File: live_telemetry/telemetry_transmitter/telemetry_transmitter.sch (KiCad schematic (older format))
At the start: 15 parts, among them J1 Programming Header, U1 PIC18F26K83, U2 MCP2562, Y1 Crystal

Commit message: Change mcu to power off 3v3 and add LRN LED/SW
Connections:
- net +5V: no longer C1.1, R1.2, U1.20 (VDD), U2.5 (VIO)
- new net +3V3: C1.1, R1.2, U1.20 (VDD), U2.5 (VIO)
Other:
- note removed: "Should VIO be 3V3 not 5V?"
- moved on the sheet: C2
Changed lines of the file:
@@
 Wire Wire Line
 	5100 3000 4700 3000
-$Comp
-L power:+5V #PWR0101
-U 1 1 5DB51D90
-P 4700 2650
-F 0 "#PWR0101" H 4700 2500 50  0001 C CNN
-F 1 "+5V" H 4715 2823 50  0000 C CNN
-F 2 "" H 4700 2650 50  0001 C CNN
-F 3 "" H 4700 2650 50  0001 C CNN
-	1    4700 2650
-	1    0    0    -1
-$EndComp
-$Comp
-L power:+5V #PWR0102
-U 1 1 5DB54163
-P 6550 2650
-F 0 "#PWR0102" H 6550 2500 50  0001 C CNN
-F 1 "+5V" H 6565 2823 50  0000 C CNN
-F 2 "" H 6550 2650 50  0001 C CNN
-F 3 "" H 6550 2650 50  0001 C CNN
-	1    6550 2650
-	1    0    0    -1
-$EndComp
 Wire Wire Line
 	4700 3000 4700 2950
@@
 L Device:C C2
 U 1 1 5DB79E78
-P 8700 5150
-F 0 "C2" H 8815 5196 50  0000 L CNN
-F 1 "10u" H 8815 5105 50  0000 L CNN
-F 2 "" H 8738 5000 50  0001 C CNN
-F 3 "~" H 8700 5150 50  0001 C CNN
-	1    8700 5150
+P 8600 5150
+F 0 "C2" H 8715 5196 50  0000 L CNN
+F 1 "10u" H 8715 5105 50  0000 L CNN
+F 2 "" H 8638 5000 50  0001 C CNN
+F 3 "~" H 8600 5150 50  0001 C CNN
+	1    8600 5150
 	1    0    0    -1
 $EndComp
@@
 L power:GND #PWR0106
 U 1 1 5DB7A312
-P 8700 5350
-F 0 "#PWR0106" H 8700 5100 50  0001 C CNN
-F 1 "GND" H 8705 5177 50  0000 C CNN
-F 2 "" H 8700 5350 50  0001 C CNN
-F 3 "" H 8700 5350 50  0001 C CNN
-	1    8700 5350
-	1    0    0    -1
-$EndComp
-Wire Wire Line
-	8700 5300 8700 5350
+P 8600 5350
+F 0 "#PWR0106" H 8600 5100 50  0001 C CNN
+F 1 "GND" H 8605 5177 50  0000 C CNN
+F 2 "" H 8600 5350 50  0001 C CNN
+F 3 "" H 8600 5350 50  0001 C CNN
+	1    8600 5350
+	1    0    0    -1
+$EndComp
+Wire Wire Line
+	8600 5300 8600 5350
 $Comp
 L power:+5V #PWR0107
 U 1 1 5DB7C40F
-P 8700 4550
-F 0 "#PWR0107" H 8700 4400 50  0001 C CNN
-F 1 "+5V" H 8715 4723 50  0000 C CNN
-F 2 "" H 8700 4550 50  0001 C CNN
-F 3 "" H 8700 4550 50  0001 C CNN
-	1    8700 4550
+P 8600 4550
+F 0 "#PWR0107" H 8600 4400 50  0001 C CNN
+F 1 "+5V" H 8615 4723 50  0000 C CNN
+F 2 "" H 8600 4550 50  0001 C CNN
+F 3 "" H 8600 4550 50  0001 C CNN
+	1    8600 4550
 	1    0    0    -1
 $EndComp
@@
 	6550 3700 8250 3700
 Wire Wire Line
-	8900 4650 8800 4650
-Wire Wire Line
-	8700 4550 8700 4650
-Connection ~ 8700 4650
-Wire Wire Line
-	8700 4650 8700 5000
+	8600 4550 8600 4650
+Connection ~ 8600 4650
+Wire Wire Line
+	8600 4650 8600 5000
 Wire Wire Line
 	8900 4750 8800 4750
-Wire Wire Line
-	8800 4750 8800 4650
-Connection ~ 8800 4650
-Wire Wire Line
-	8800 4650 8700 4650
 $Comp
 L power:+5V #PWR0110
@@
 Wire Wire Line
 	2000 3400 2000 3200
-Text Notes 8850 5400 0    50   ~ 0
-Should VIO be 3V3 not 5V?
 Text Label 4550 3000 2    50   ~ 0
 ~MCLR
@@
 Text Notes 7100 6950 0    50   ~ 0
 The purpose of the telemetry transmitter board is to take in data from\n the can bus and transmit this data to the telemetry receiver board. \nThe telemetry transmitter board will then transmit this data via a RF module.
+$Comp
+L power:+3V3 #PWR0101
+U 1 1 5DE42E6B
+P 4700 2650
+F 0 "#PWR0101" H 4700 2500 50  0001 C CNN
+F 1 "+3V3" H 4715 2823 50  0000 C CNN
+F 2 "" H 4700 2650 50  0001 C CNN
+F 3 "" H 4700 2650 50  0001 C CNN
+	1    4700 2650
+	1    0    0    -1
+$EndComp
+$Comp
+L power:+3V3 #PWR0102
+U 1 1 5DE4639A
+P 6550 2650
+F 0 "#PWR0102" H 6550 2500 50  0001 C CNN
+F 1 "+3V3" H 6565 2823 50  0000 C CNN
+F 2 "" H 6550 2650 50  0001 C CNN
+F 3 "" H 6550 2650 50  0001 C CNN
+	1    6550 2650
+	1    0    0    -1
+$EndComp
+$Comp
+L power:+3V3 #PWR0126
+U 1 1 5DE483B0
+P 8800 4550
+F 0 "#PWR0126" H 8800 4400 50  0001 C CNN
+F 1 "+3V3" H 8815 4723 50  0000 C CNN
+F 2 "" H 8800 4550 50  0001 C CNN
+F 3 "" H 8800 4550 50  0001 C CNN
+	1    8800 4550
+	1    0    0    -1
+$EndComp
+Wire Wire Line
+	8600 4650 8900 4650
+Wire Wire Line
+	8800 4550 8800 4750
 $EndSCHEMATC

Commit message: Fix voltage mismatches, LED voltages, and add relative file path for canlib
-Programming header switched from 5V to 3V3
-LEDs switched from 5V to 3V3
-Relative file path added for transmitter and receiver for canlib
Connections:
- net +3V3: now also D1.2 (A), D2.2 (A), D3.2 (A), J1.4 (Pin_4)
- net +5V: no longer D1.2 (A), D2.2 (A), D3.2 (A), J1.4 (Pin_4)
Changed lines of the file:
@@
 EESchema Schematic File Version 4
+LIBS:telemetry_transmitter-cache
 EELAYER 29 0
 EELAYER END
@@
 Wire Wire Line
 	8900 4750 8800 4750
-$Comp
-L power:+5V #PWR0110
-U 1 1 5DC7920B
-P 2400 1700
-F 0 "#PWR0110" H 2400 1550 50  0001 C CNN
-F 1 "+5V" H 2415 1873 50  0000 C CNN
-F 2 "" H 2400 1700 50  0001 C CNN
-F 3 "" H 2400 1700 50  0001 C CNN
-	1    2400 1700
-	1    0    0    -1
-$EndComp
 Wire Wire Line
 	2050 2050 2400 2050
@@
 	0    -1   -1   0
 $EndComp
-$Comp
-L power:+5V #PWR0111
-U 1 1 5DC96631
-P 2350 3150
-F 0 "#PWR0111" H 2350 3000 50  0001 C CNN
-F 1 "+5V" H 2365 3323 50  0000 C CNN
-F 2 "" H 2350 3150 50  0001 C CNN
-F 3 "" H 2350 3150 50  0001 C CNN
-	1    2350 3150
-	1    0    0    -1
-$EndComp
-Wire Wire Line
-	2000 3400 2000 3200
 Text Label 4550 3000 2    50   ~ 0
 ~MCLR
@@
 Wire Wire Line
 	2350 3200 2350 3400
-Wire Wire Line
-	2000 3200 2350 3200
 Wire Wire Line
 	2700 3400 2700 3200
@@
 Wire Wire Line
 	8800 4550 8800 4750
+$Comp
+L power:+3V3 #PWR?
+U 1 1 5E043275
+P 2350 3150
+F 0 "#PWR?" H 2350 3000 50  0001 C CNN
+F 1 "+3V3" H 2365 3323 50  0000 C CNN
+F 2 "" H 2350 3150 50  0001 C CNN
+F 3 "" H 2350 3150 50  0001 C CNN
+	1    2350 3150
+	1    0    0    -1
+$EndComp
+$Comp
+L power:+3V3 #PWR?
+U 1 1 5E04875A
+P 2400 1700
+F 0 "#PWR?" H 2400 1550 50  0001 C CNN
+F 1 "+3V3" H 2415 1873 50  0000 C CNN
+F 2 "" H 2400 1700 50  0001 C CNN
+F 3 "" H 2400 1700 50  0001 C CNN
+	1    2400 1700
+	1    0    0    -1
+$EndComp
+Wire Wire Line
+	2000 3400 2000 3200
+Wire Wire Line
+	2000 3200 2350 3200
 $EndSCHEMATC

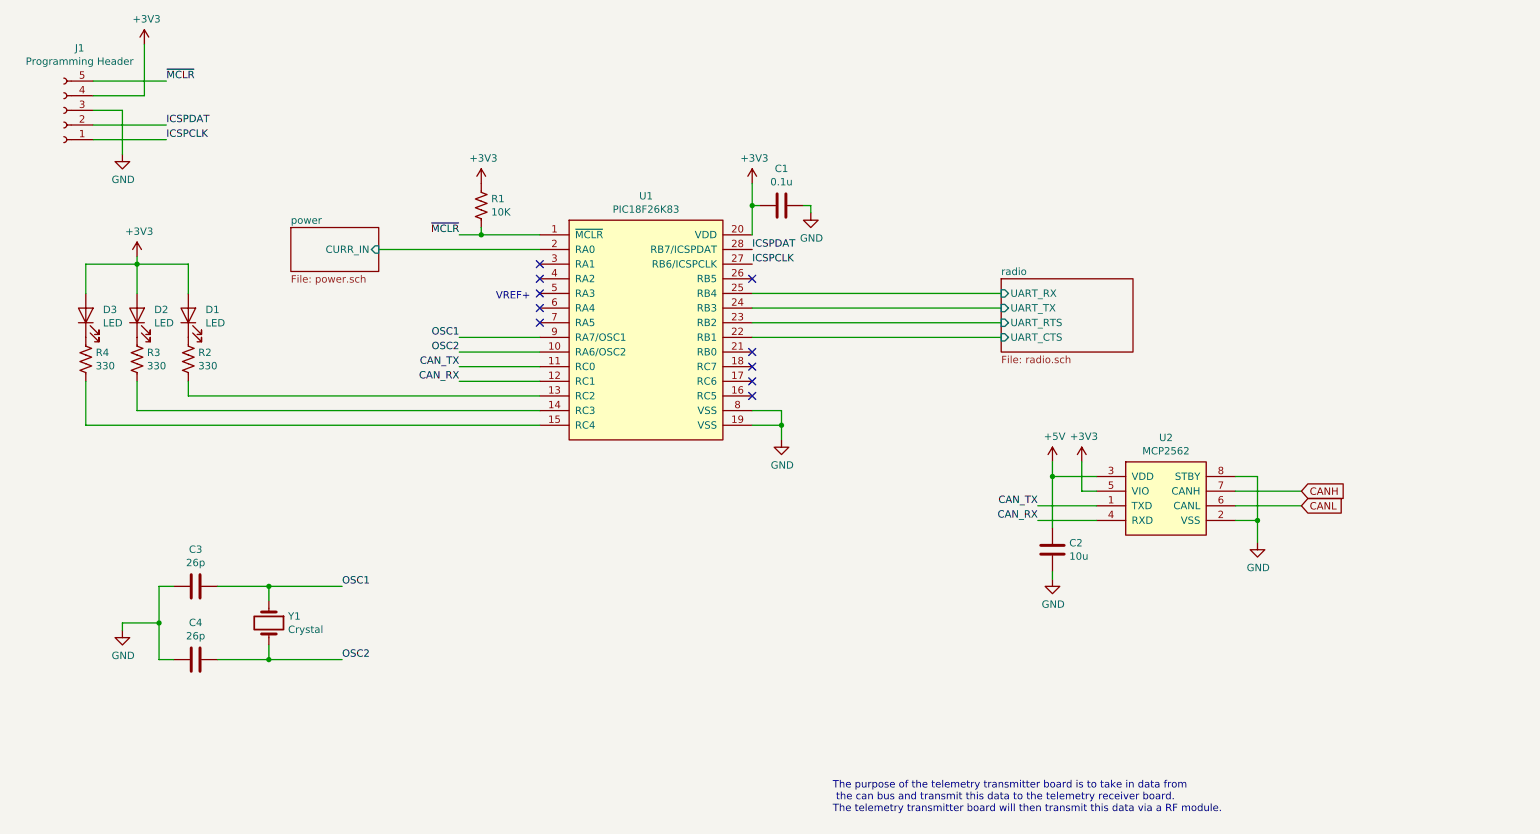
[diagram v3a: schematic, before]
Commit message: Addresses Adam/Aaron's comments: change RF module and take over for radio
Now that the CAN bus battery is going in the recovery electronics bay,
the telemetry_transmitter board will be taking over for radio for all
communication from RLCS to the rocket and will also handle the power
control of the CAN bus.
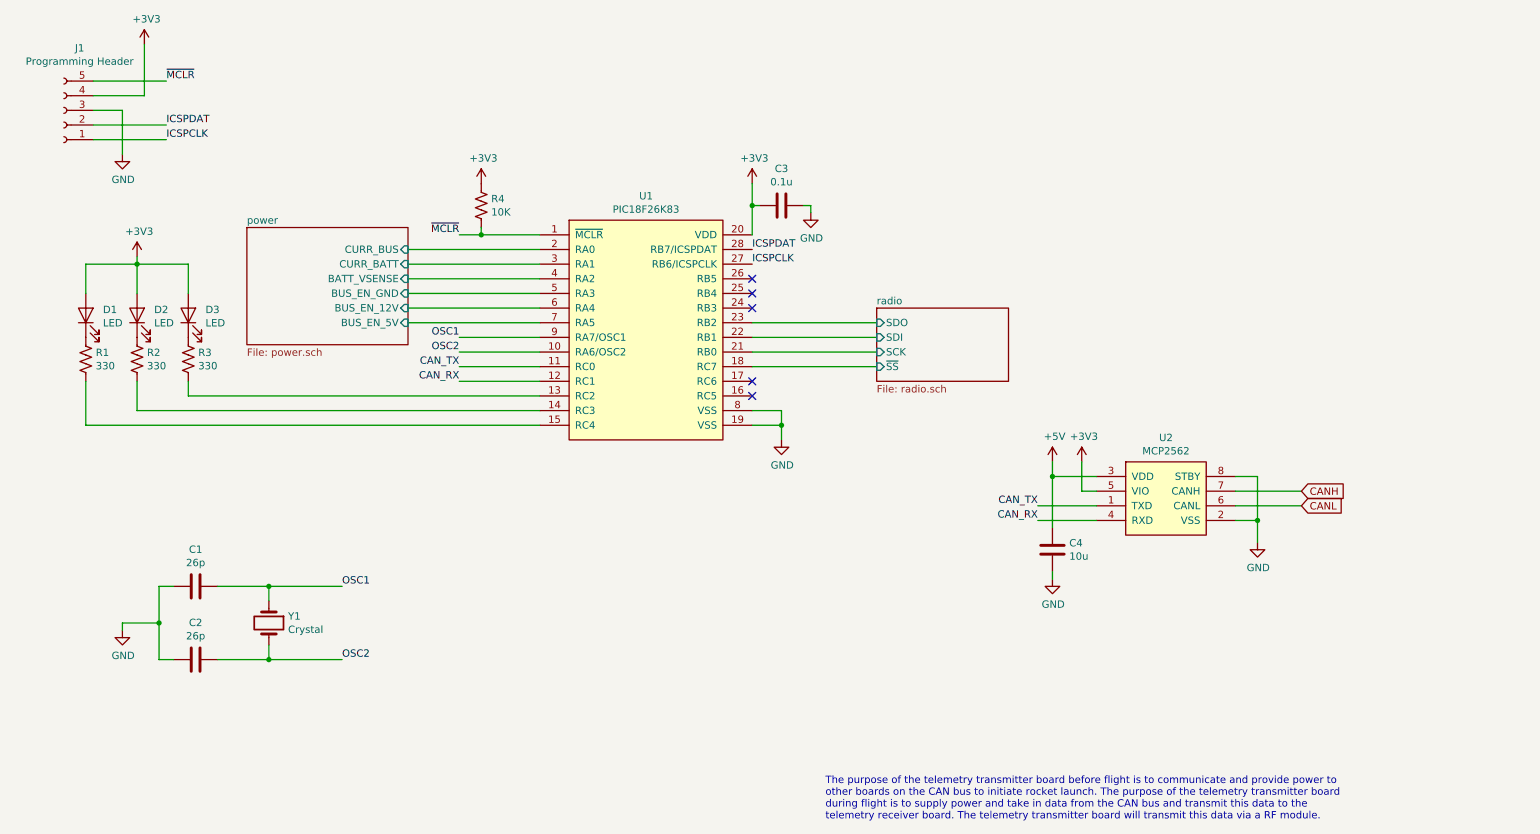
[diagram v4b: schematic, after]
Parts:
- renumbered C3 to C1, C4 to C2, C1 to C3, C2 to C4, D3 to D1, D1 to D3, R4 to R1, R3 to R2, R2 to R3, R1 to R4
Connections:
- net radio/~SS: now reaches U1.18 (RC7)
- net radio/SCK: now reaches U1.21 (RB0)
- net power/CURR_BATT: now reaches U1.3 (RA1)
- net power/BATT_VSENSE: now reaches U1.4 (RA2)
- net power/BUS_EN_GND: now reaches U1.5 (RA3)
- net power/BUS_EN_12V: now reaches U1.6 (RA4)
- net power/BUS_EN_5V: now reaches U1.7 (RA5)
- net power/CURR_IN renamed power/CURR_BUS
- net radio/UART_CTS renamed radio/SDI
- net radio/UART_RTS renamed radio/SDO
- net radio/UART_RX: no longer names the net of U1.25 (RB4)
- net radio/UART_TX: no longer names the net of U1.24 (RB3)
- no-connect marks 10 -> 5
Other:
- note added: "The purpose of the telemetry transmitter board before flight is to communicate and provide power to \nother boards on the CAN bus to initiate rocket launch. The purpose of the telemetry transmitter board\nduring flight is to supply power and take in data from the CAN bus and transmit this data to the \ntelemetry receiver board. The telemetry transmitter board will transmit this data via a RF modu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"
- note removed: "The purpose of the telemetry transmitter board is to take in data from\n the can bus and transmit this data to the telemetry receiver board. \nThe telemetry transmitter board will then transmit this data via a RF module."
- note removed: "VREF+"
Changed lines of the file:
@@
 	4700 3000 4700 2950
 $Comp
-L Device:C C1
+L Device:C C3
 U 1 1 5DB55931
 P 6750 2800
-F 0 "C1" V 7002 2800 50  0000 C CNN
+F 0 "C3" V 7002 2800 50  0000 C CNN
 F 1 "0.1u" V 6911 2800 50  0000 C CNN
 F 2 "" H 6788 2650 50  0001 C CNN
@@
 Connection ~ 6550 2800
 $Comp
-L power:GND #PWR0103
+L power:GND #PWR08
 U 1 1 5DB58627
 P 6950 2850
-F 0 "#PWR0103" H 6950 2600 50  0001 C CNN
+F 0 "#PWR08" H 6950 2600 50  0001 C CNN
 F 1 "GND" H 6955 2677 50  0000 C CNN
 F 2 "" H 6950 2850 50  0001 C CNN
@@
 	6950 2800 6900 2800
 $Comp
-L Device:R_US R1
+L Device:R_US R4
 U 1 1 5DB60B01
 P 4700 2800
-F 0 "R1" H 4632 2754 50  0000 R CNN
+F 0 "R4" H 4632 2754 50  0000 R CNN
 F 1 "10K" H 4632 2845 50  0000 R CNN
 F 2 "" V 4740 2790 50  0001 C CNN
@@
 $EndComp
 $Comp
-L power:GND #PWR0104
+L power:GND #PWR07
 U 1 1 5DB64327
 P 6750 4400
-F 0 "#PWR0104" H 6750 4150 50  0001 C CNN
+F 0 "#PWR07" H 6750 4150 50  0001 C CNN
 F 1 "GND" H 6755 4227 50  0000 C CNN
 F 2 "" H 6750 4400 50  0001 C CNN
@@
 Text Label 6550 3200 0    50   ~ 0
 ICSPCLK
-NoConn ~ 5100 3400
-Text Notes 4800 3450 0    50   ~ 0
-VREF+
 Text Label 4550 3700 2    50   ~ 0
 OSC1
@@
 ICSPCLK
 $Comp
-L power:GND #PWR0105
+L power:GND #PWR01
 U 1 1 5DB6C1BD
 P 2250 2450
-F 0 "#PWR0105" H 2250 2200 50  0001 C CNN
+F 0 "#PWR01" H 2250 2200 50  0001 C CNN
 F 1 "GND" H 2255 2277 50  0000 C CNN
 F 2 "" H 2250 2450 50  0001 C CNN
@@
 	9850 4850 10300 4850
 $Comp
-L Device:C C2
+L Device:C C4
 U 1 1 5DB79E78
 P 8600 5150
-F 0 "C2" H 8715 5196 50  0000 L CNN
+F 0 "C4" H 8715 5196 50  0000 L CNN
 F 1 "10u" H 8715 5105 50  0000 L CNN
 F 2 "" H 8638 5000 50  0001 C CNN
@@
 $EndComp
 $Comp
-L power:GND #PWR0106
+L power:GND #PWR010
 U 1 1 5DB7A312
 P 8600 5350
-F 0 "#PWR0106" H 8600 5100 50  0001 C CNN
+F 0 "#PWR010" H 8600 5100 50  0001 C CNN
 F 1 "GND" H 8605 5177 50  0000 C CNN
 F 2 "" H 8600 5350 50  0001 C CNN
@@
 	8600 5300 8600 5350
 $Comp
-L power:+5V #PWR0107
+L power:+5V #PWR09
 U 1 1 5DB7C40F
 P 8600 4550
-F 0 "#PWR0107" H 8600 4400 50  0001 C CNN
+F 0 "#PWR09" H 8600 4400 50  0001 C CNN
 F 1 "+5V" H 8615 4723 50  0000 C CNN
 F 2 "" H 8600 4550 50  0001 C CNN
@@
 $EndComp
 $Comp
-L Device:C C3
+L Device:C C1
 U 1 1 5DB888B6
 P 2750 5400
-F 0 "C3" V 2498 5400 50  0000 C CNN
+F 0 "C1" V 2498 5400 50  0000 C CNN
 F 1 "26p" V 2589 5400 50  0000 C CNN
 F 2 "" H 2788 5250 50  0001 C CNN
@@
 $EndComp
 $Comp
-L Device:C C4
+L Device:C C2
 U 1 1 5DB89801
 P 2750 5900
-F 0 "C4" V 2498 5900 50  0000 C CNN
+F 0 "C2" V 2498 5900 50  0000 C CNN
 F 1 "26p" V 2589 5900 50  0000 C CNN
 F 2 "" H 2788 5750 50  0001 C CNN
@@
 	3250 5500 3250 5400
 $Comp
-L power:GND #PWR0108
+L power:GND #PWR02
 U 1 1 5DB8CF15
 P 2250 5700
-F 0 "#PWR0108" H 2250 5450 50  0001 C CNN
+F 0 "#PWR02" H 2250 5450 50  0001 C CNN
 F 1 "GND" H 2255 5527 50  0000 C CNN
 F 2 "" H 2250 5700 50  0001 C CNN
@@
 	10000 4950 10000 5100
 $Comp
-L power:GND #PWR0109
+L power:GND #PWR012
 U 1 1 5DB74F13
 P 10000 5100
-F 0 "#PWR0109" H 10000 4850 50  0001 C CNN
+F 0 "#PWR012" H 10000 4850 50  0001 C CNN
 F 1 "GND" H 10005 4927 50  0000 C CNN
 F 2 "" H 10000 5100 50  0001 C CNN
@@
 $EndComp
 Wire Wire Line
-	6550 3400 8250 3400
-Wire Wire Line
-	6550 3500 8250 3500
-Wire Wire Line
-	6550 3600 8250 3600
-Wire Wire Line
-	6550 3700 8250 3700
-Wire Wire Line
 	8600 4550 8600 4650
 Connection ~ 8600 4650
@@
 	2400 2050 2400 1700
 $Comp
-L Device:R_US R4
+L Device:R_US R1
 U 1 1 5DC8311E
 P 2000 3850
-F 0 "R4" H 2068 3896 50  0000 L CNN
+F 0 "R1" H 2068 3896 50  0000 L CNN
 F 1 "330" H 2068 3805 50  0000 L CNN
 F 2 "" V 2040 3840 50  0001 C CNN
@@
 $EndComp
 $Comp
-L Device:R_US R3
+L Device:R_US R2
 U 1 1 5DC8654A
 P 2350 3850
-F 0 "R3" H 2418 3896 50  0000 L CNN
+F 0 "R2" H 2418 3896 50  0000 L CNN
 F 1 "330" H 2418 3805 50  0000 L CNN
 F 2 "" V 2390 3840 50  0001 C CNN
@@
 $EndComp
 $Comp
-L Device:R_US R2
+L Device:R_US R3
 U 1 1 5DC87619
 P 2700 3850
-F 0 "R2" H 2768 3896 50  0000 L CNN
+F 0 "R3" H 2768 3896 50  0000 L CNN
 F 1 "330" H 2768 3805 50  0000 L CNN
 F 2 "" V 2740 3840 50  0001 C CNN
@@
 	2000 4300 2000 4000
 $Comp
-L Device:LED D3
+L Device:LED D1
 U 1 1 5DC9255B
 P 2000 3550
-F 0 "D3" V 2039 3433 50  0000 R CNN
+F 0 "D1" V 2039 3433 50  0000 R CNN
 F 1 "LED" V 1948 3433 50  0000 R CNN
 F 2 "" H 2000 3550 50  0001 C CNN
@@
 $EndComp
 $Comp
-L Device:LED D1
+L Device:LED D3
 U 1 1 5DC950BA
 P 2700 3550
-F 0 "D1" V 2739 3433 50  0000 R CNN
+F 0 "D3" V 2739 3433 50  0000 R CNN
 F 1 "LED" V 2648 3433 50  0000 R CNN
 F 2 "" H 2700 3550 50  0001 C CNN
@@
 Wire Wire Line
 	6550 2650 6550 2800
-$Sheet
-S 3400 2950 600  300
-U 5DCE01AA
-F0 "power" 50
-F1 "power.sch" 50
-F2 "CURR_IN" I R 4000 3100 50
-$EndSheet
-Wire Wire Line
-	4000 3100 5100 3100
-$Sheet
-S 8250 3300 900  500
-U 5DCEE789
-F0 "radio" 50
-F1 "radio.sch" 50
-F2 "UART_RX" I L 8250 3400 50
-F3 "UART_TX" I L 8250 3500 50
-F4 "UART_CTS" I L 8250 3700 50
-F5 "UART_RTS" I L 8250 3600 50
-$EndSheet
 Wire Wire Line
 	2350 3150 2350 3200
@@
 Wire Wire Line
 	2700 3200 2350 3200
-NoConn ~ 5100 3200
-NoConn ~ 5100 3300
-NoConn ~ 5100 3500
-NoConn ~ 5100 3600
-NoConn ~ 6550 3800
-NoConn ~ 6550 3900
 NoConn ~ 6550 4000
 NoConn ~ 6550 4100
 NoConn ~ 6550 3300
-Text Notes 7100 6950 0    50   ~ 0
-The purpose of the telemetry transmitter board is to take in data from\n the can bus and transmit this data to the telemetry receiver board. \nThe telemetry transmitter board will then transmit this data via a RF module.
-$Comp
-L power:+3V3 #PWR0101
+Text Notes 7050 7000 0    50   ~ 0
+The purpose of the telemetry transmitter board before flight is to communicate and provide power to \nother boards on the CAN bus to initiate rocket launch. The purpose of the telemetry transmitter board\nduring flight is to supply power and take in data from the CAN bus and transmit this data to the \ntelemetry receiver board. The telemetry transmitter board will transmit this data via a RF module.
+$Comp
+L power:+3V3 #PWR05
 U 1 1 5DE42E6B
 P 4700 2650
-F 0 "#PWR0101" H 4700 2500 50  0001 C CNN
+F 0 "#PWR05" H 4700 2500 50  0001 C CNN
 F 1 "+3V3" H 4715 2823 50  0000 C CNN
 F 2 "" H 4700 2650 50  0001 C CNN
@@
 $EndComp
 $Comp
-L power:+3V3 #PWR0102
+L power:+3V3 #PWR06
 U 1 1 5DE4639A
 P 6550 2650
-F 0 "#PWR0102" H 6550 2500 50  0001 C CNN
+F 0 "#PWR06" H 6550 2500 50  0001 C CNN
 F 1 "+3V3" H 6565 2823 50  0000 C CNN
 F 2 "" H 6550 2650 50  0001 C CNN
@@
 $EndComp
 $Comp
-L power:+3V3 #PWR0126
+L power:+3V3 #PWR011
 U 1 1 5DE483B0
 P 8800 4550
-F 0 "#PWR0126" H 8800 4400 50  0001 C CNN
+F 0 "#PWR011" H 8800 4400 50  0001 C CNN
 F 1 "+3V3" H 8815 4723 50  0000 C CNN
 F 2 "" H 8800 4550 50  0001 C CNN
@@
 	8800 4550 8800 4750
 $Comp
-L power:+3V3 #PWR?
+L power:+3V3 #PWR03
 U 1 1 5E043275
 P 2350 3150
-F 0 "#PWR?" H 2350 3000 50  0001 C CNN
+F 0 "#PWR03" H 2350 3000 50  0001 C CNN
 F 1 "+3V3" H 2365 3323 50  0000 C CNN
 F 2 "" H 2350 3150 50  0001 C CNN
@@
 $EndComp
 $Comp
-L power:+3V3 #PWR?
+L power:+3V3 #PWR04
 U 1 1 5E04875A
 P 2400 1700
-F 0 "#PWR?" H 2400 1550 50  0001 C CNN
+F 0 "#PWR04" H 2400 1550 50  0001 C CNN
 F 1 "+3V3" H 2415 1873 50  0000 C CNN
 F 2 "" H 2400 1700 50  0001 C CNN
@@
 Wire Wire Line
 	2000 3200 2350 3200
+$Sheet
+S 3100 2950 1100 800
+U 5E2687EB
+F0 "power" 50
+F1 "power.sch" 50
+F2 "CURR_BUS" I R 4200 3100 50
+F3 "CURR_BATT" I R 4200 3200 50
+F4 "BATT_VSENSE" I R 4200 3300 50
+F5 "BUS_EN_GND" I R 4200 3400 50
+F6 "BUS_EN_12V" I R 4200 3500 50
+F7 "BUS_EN_5V" I R 4200 3600 50
+$EndSheet
+Wire Wire Line
+	4200 3100 5100 3100
+Wire Wire Line
+	5100 3200 4200 3200
+Wire Wire Line
+	4200 3300 5100 3300
+Wire Wire Line
+	4200 3400 5100 3400
+Wire Wire Line
+	4200 3500 5100 3500
+Wire Wire Line
+	4200 3600 5100 3600
+$Sheet
+S 7400 3500 900  500
+U 5E28F6B3
+F0 "radio" 50
+F1 "radio.sch" 50
+F2 "~SS" I L 7400 3900 50
+F3 "SCK" I L 7400 3800 50
+F4 "SDI" I L 7400 3700 50
+F5 "SDO" I L 7400 3600 50
+$EndSheet
+Wire Wire Line
+	6550 3900 7400 3900
+Wire Wire Line
+	7400 3800 6550 3800
+Wire Wire Line
+	6550 3700 7400 3700
+Wire Wire Line
+	6550 3600 7400 3600
+NoConn ~ 6550 3400
+NoConn ~ 6550 3500
 $EndSCHEMATC

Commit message: Address Zach/Aaron's comments for resistor values, CAN bus power, and reset pin
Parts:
- R1, R2, R3: value 330 -> 130
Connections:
- net radio/RESET: now reaches U1.17 (RC6)
- no-connect marks 5 -> 4
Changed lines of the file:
@@
 P 2000 3850
 F 0 "R1" H 2068 3896 50  0000 L CNN
-F 1 "330" H 2068 3805 50  0000 L CNN
+F 1 "130" H 2068 3805 50  0000 L CNN
 F 2 "" V 2040 3840 50  0001 C CNN
 F 3 "~" H 2000 3850 50  0001 C CNN
@@
 P 2350 3850
 F 0 "R2" H 2418 3896 50  0000 L CNN
-F 1 "330" H 2418 3805 50  0000 L CNN
+F 1 "130" H 2418 3805 50  0000 L CNN
 F 2 "" V 2390 3840 50  0001 C CNN
 F 3 "~" H 2350 3850 50  0001 C CNN
@@
 P 2700 3850
 F 0 "R3" H 2768 3896 50  0000 L CNN
-F 1 "330" H 2768 3805 50  0000 L CNN
+F 1 "130" H 2768 3805 50  0000 L CNN
 F 2 "" V 2740 3840 50  0001 C CNN
 F 3 "~" H 2700 3850 50  0001 C CNN
@@
 Wire Wire Line
 	2700 3200 2350 3200
-NoConn ~ 6550 4000
 NoConn ~ 6550 4100
 NoConn ~ 6550 3300
@@
 Wire Wire Line
 	4200 3600 5100 3600
+Wire Wire Line
+	6550 3900 7400 3900
+Wire Wire Line
+	7400 3800 6550 3800
+Wire Wire Line
+	6550 3700 7400 3700
+Wire Wire Line
+	6550 3600 7400 3600
+NoConn ~ 6550 3400
+NoConn ~ 6550 3500
 $Sheet
-S 7400 3500 900  500
-U 5E28F6B3
+S 7400 3500 850  600
+U 5E233576
 F0 "radio" 50
 F1 "radio.sch" 50
@@
 F4 "SDI" I L 7400 3700 50
 F5 "SDO" I L 7400 3600 50
+F6 "RESET" I L 7400 4000 50
 $EndSheet
 Wire Wire Line
-	6550 3900 7400 3900
-Wire Wire Line
-	7400 3800 6550 3800
-Wire Wire Line
-	6550 3700 7400 3700
-Wire Wire Line
-	6550 3600 7400 3600
-NoConn ~ 6550 3400
-NoConn ~ 6550 3500
+	6550 4000 7400 4000
 $EndSCHEMATC
